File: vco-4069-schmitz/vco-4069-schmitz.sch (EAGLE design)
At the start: 35 parts, among them IC1 4069N, Q1 BC560, Q2 BC550B, Q3 BC550B

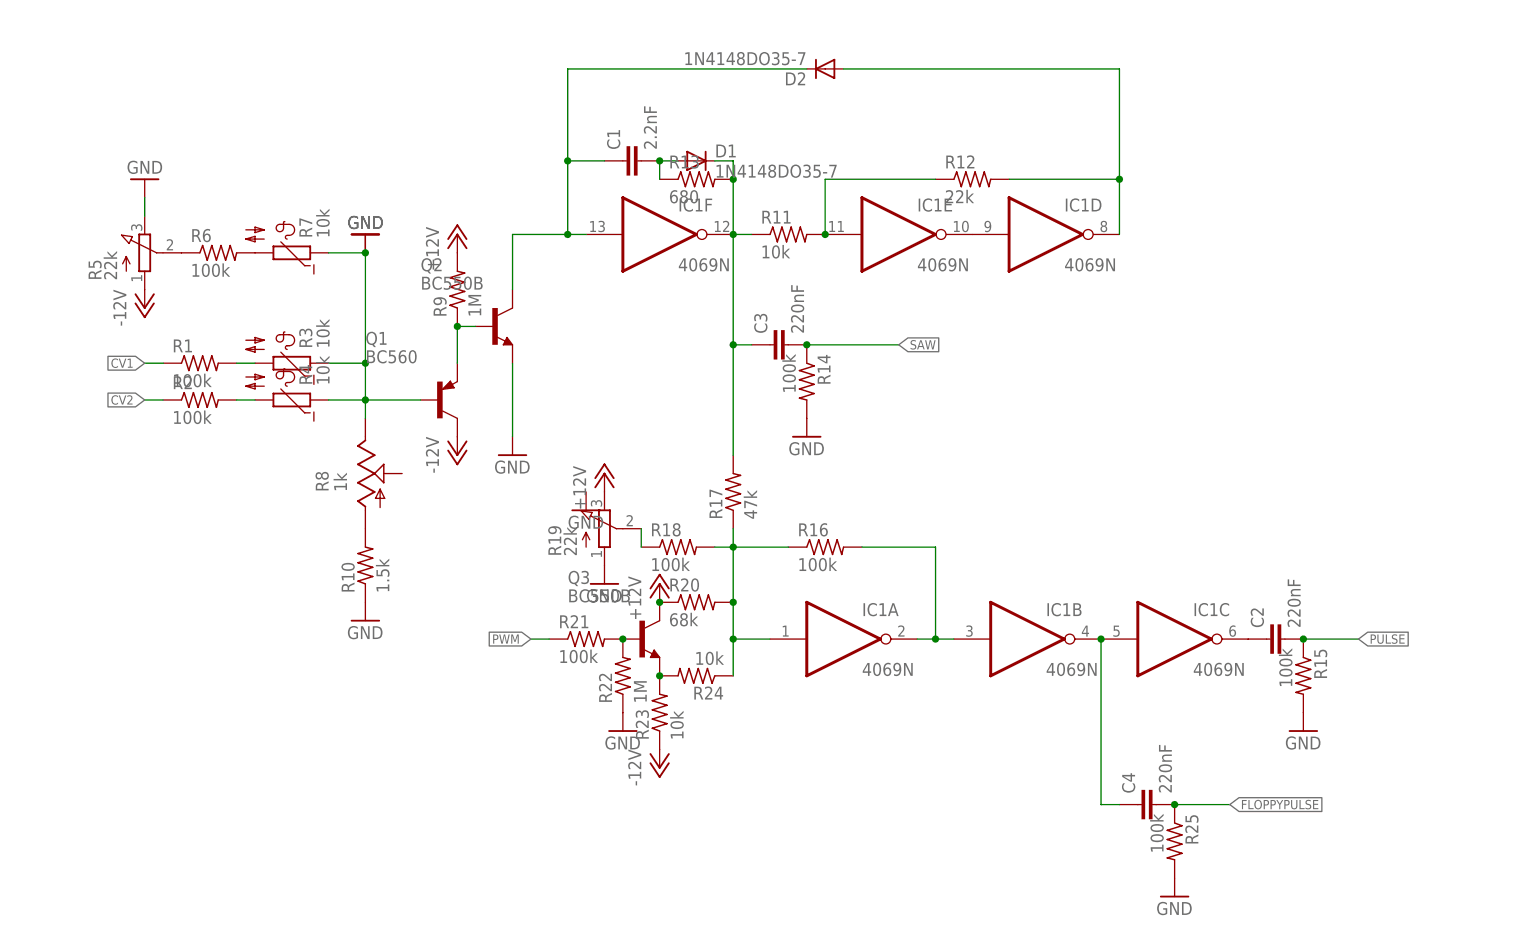
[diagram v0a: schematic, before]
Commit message: Schmitz VCO board
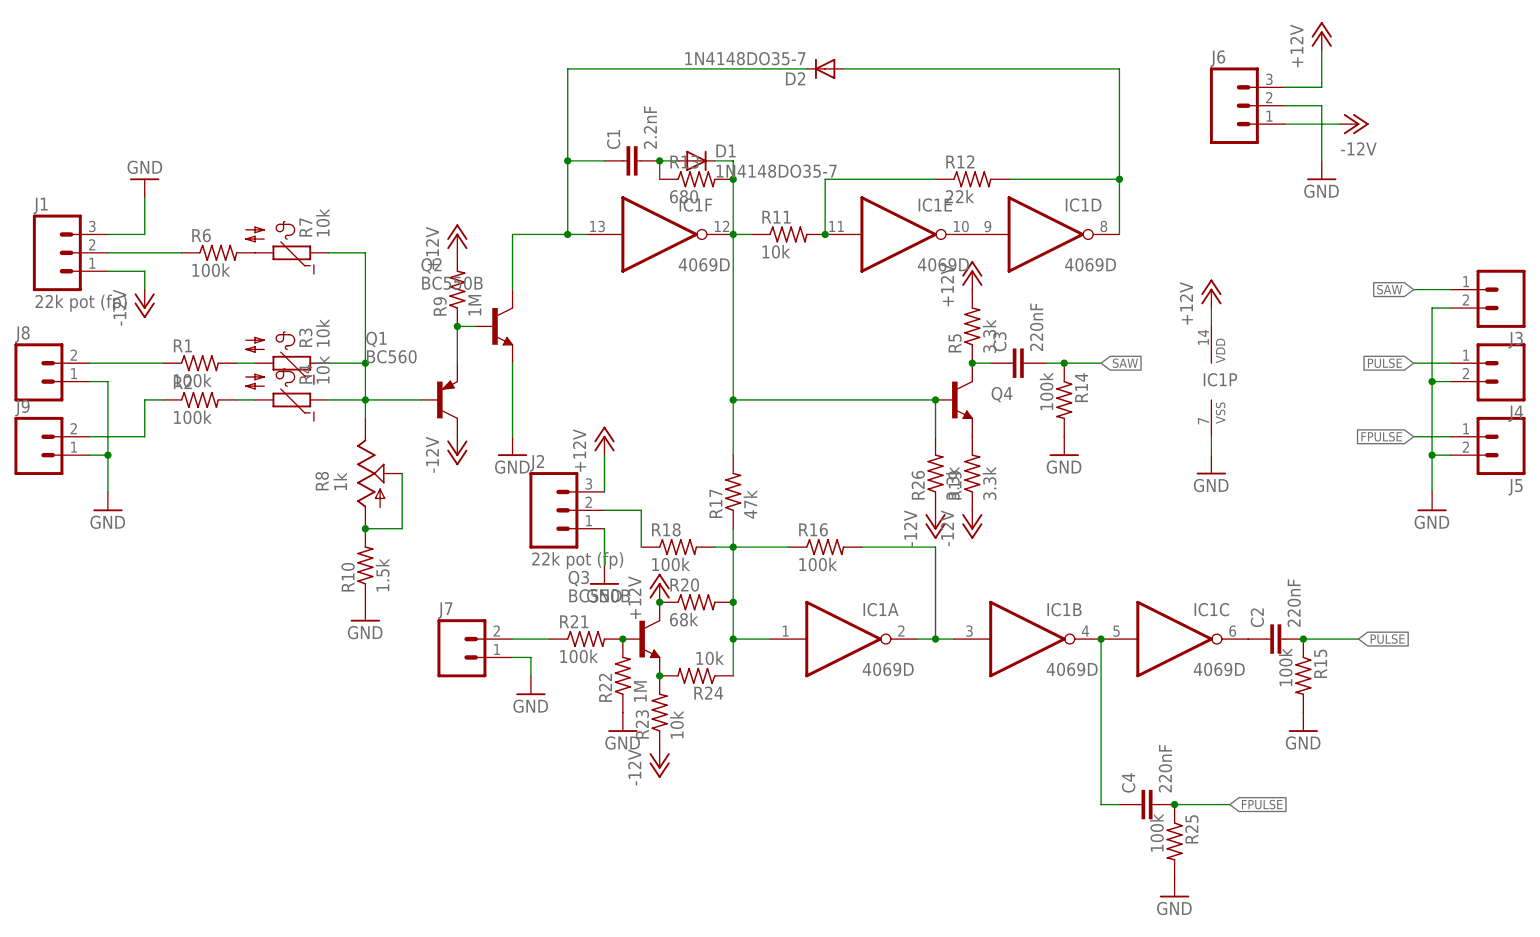
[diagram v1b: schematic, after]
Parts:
- added J1, J2: 22k pot (fp), SparkFun-Connectors:M03PTH
- added J3, J4, J5, J7, J8, J9: (no value), SparkFun-Connectors:M02PTH
- added J6: (no value), SparkFun-Connectors:M03PTH
- added Q4: (no value), SparkFun-DiscreteSemi:TRANSISTOR_NPNMMBT2222A
- added R26: 3.3k, resistor:R-US_R0805
- C1, C2, C3, C4: device resistor:C-EU025-025X050 -> resistor:C-EUC0805
- IC1: value 4069N -> 4069D; device 40xx:4069N -> 40xx:4069D
- R1, R10, R11, R12, R13, R14, R15, R16, R17, R18, R2, R20, R21, R22, R23, R24, R25, R6, R9: device resistor:R-US_0204/2V -> resistor:R-US_R0805
- R19, R5: value 22k -> 3.3k; device pot:3RP/1610N -> resistor:R-US_R0805
- R8: device pot:TRIM_US-LI15 -> pot:TRIM_US-B25P
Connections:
- removed net +15V: R19.E
- removed net CV1: R1.1
- removed net FLOPPYPULSE: C4.2, R25.1
- removed net PWM: R21.1
- new net FPULSE: C4.2, J5.1, R25.1
- new net N$20: Q1.B, R3.1, R4.1, R7.1, R8.E
- new net N$21: J7.2, R21.1
- new net N$22: J8.2, R1.1
- new net N$23: C3.1, Q4.C, R5.1
- new net N$25: D1.C, IC1F.O, Q4.B, R11.1, R13.2, R17.2, R26.2
- net +12V: now also IC1P.VDD, J2.3, J6.3, R5.2
- net -12V: now also J1.1, J6.1, R19.1, R26.1; no longer R5.A
- net CV2: now also J9.2
- net GND: now also IC1P.VSS, J1.3, J2.1, J3.2, J4.2, J5.2, J6.2, J7.1, J8.1, J9.1; no longer Q1.B, R19.A, R3.1, R4.1, R5.E, R7.1, R8.E
- net N$1: now also J1.2; no longer R5.S
- net N$14: now also Q4.E, R19.2; no longer C3.1, D1.C, IC1F.O, R11.1, R13.2, R17.2
- net N$18: now also J2.2; no longer R19.S
- net N$7: now also R8.S
- net PULSE: now also J4.1
- net SAW: now also J3.1
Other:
- moved on the sheet: C3, R14
